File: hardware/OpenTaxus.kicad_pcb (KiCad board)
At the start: 2 copper layers, 66.7 x 85.7 mm, 54 parts, among them J1 OLED, J2 qwiic, J3 SWD, J4 USB_C_Receptacle_USB2.0, Q2 BC847BS, Q3 PT12-21B/TR8, SW1 dpad, SW2 USB_BOOT, SW3 RESET, SW4 SW_SPDT, U1 HE6206-33NR, U2 W25Q128JVS, U3 RP2040, U4 XT1861B332MR-G, Y1 YSX321SL

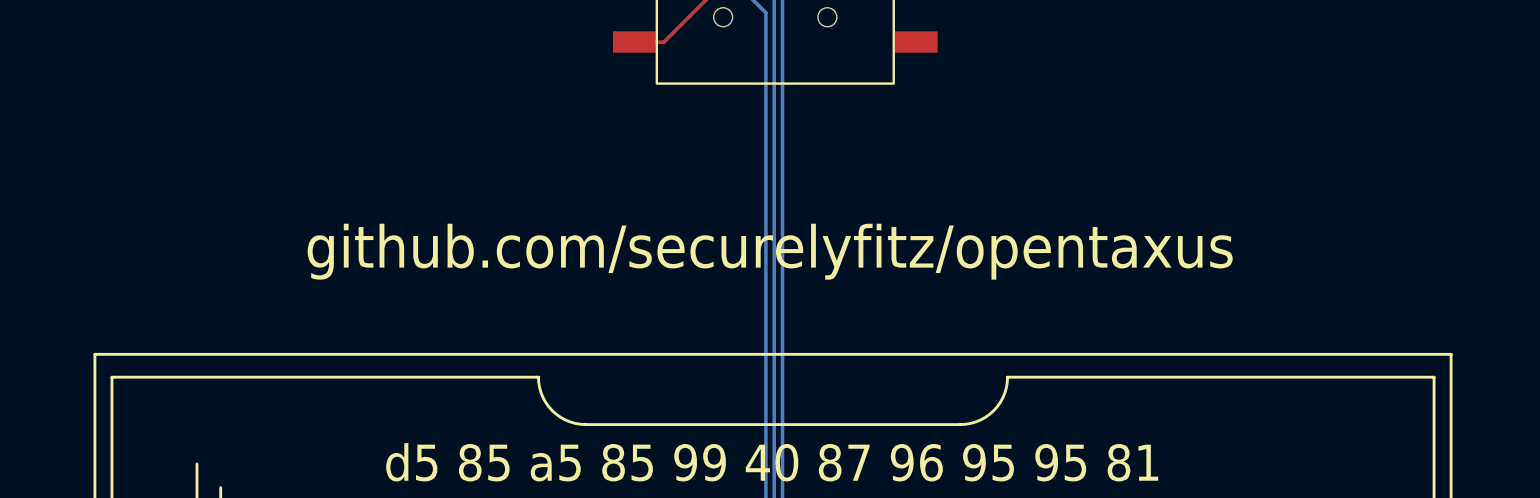
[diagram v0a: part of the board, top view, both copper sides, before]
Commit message: updating to kicad 9
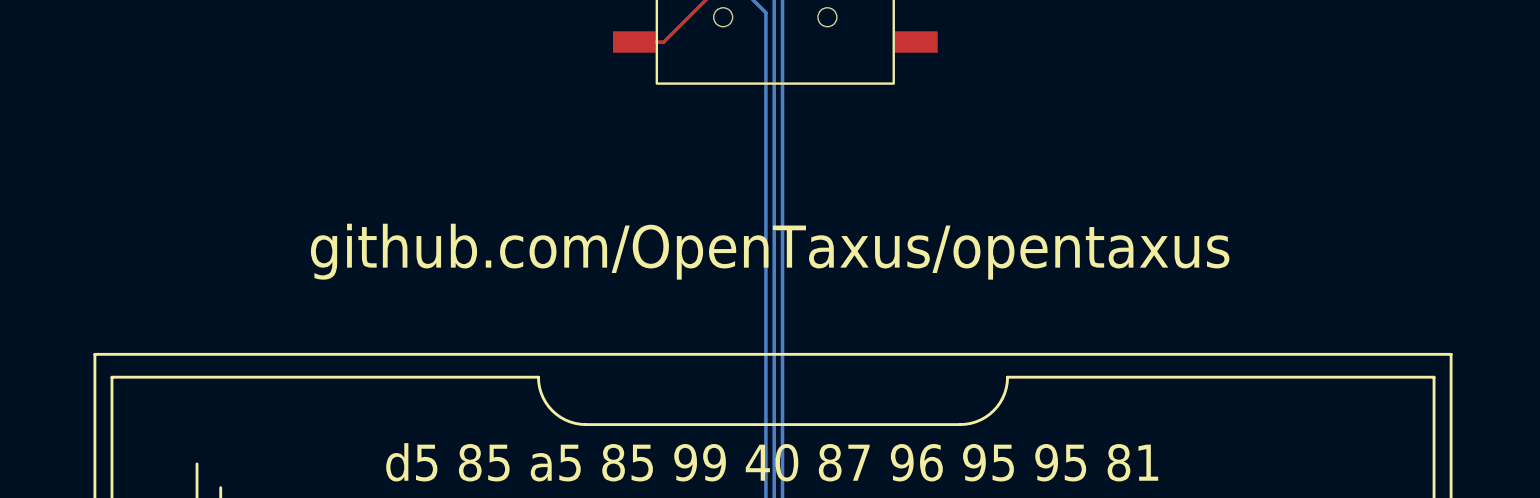
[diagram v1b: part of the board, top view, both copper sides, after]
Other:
- board text added: "github.com/OpenTaxus/opentaxus"
- board text removed: "github.com/securelyfitz/opentaxus"
